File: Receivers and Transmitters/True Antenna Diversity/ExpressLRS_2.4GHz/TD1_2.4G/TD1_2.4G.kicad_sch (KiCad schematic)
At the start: 8 parts, among them J1 Conn_01x04_Pin, J2 Conn_01x04_Socket, U1 TPS7A4701xRGW

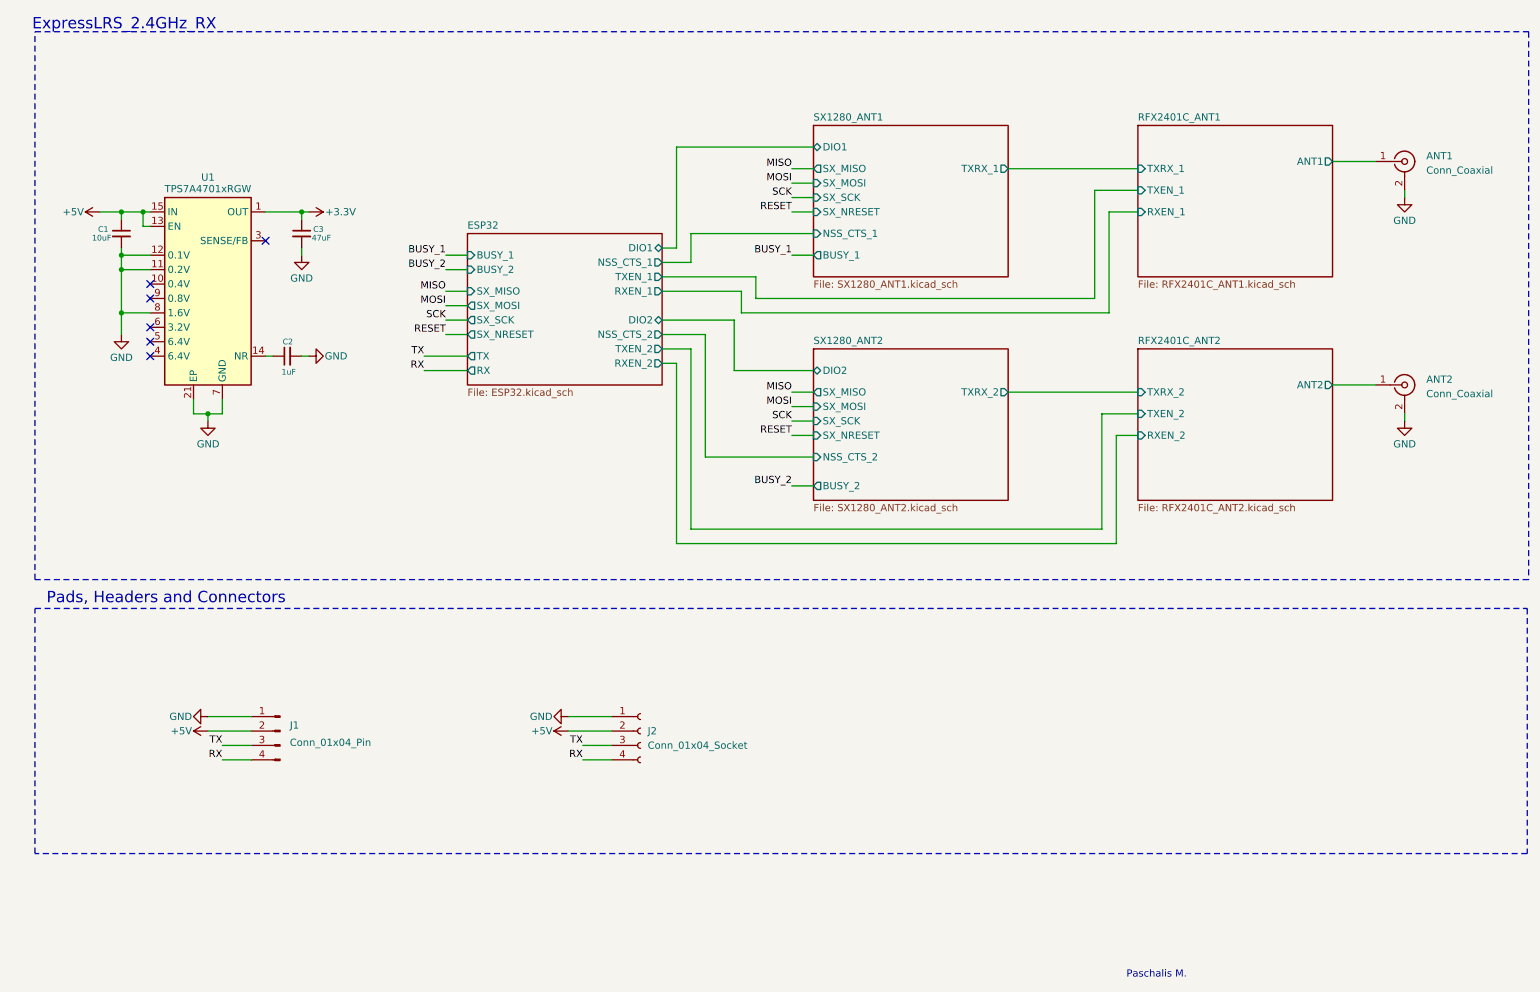
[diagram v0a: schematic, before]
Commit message: Update True Antenna Diversity TD1_2.4G KiCad schematics and PCB design
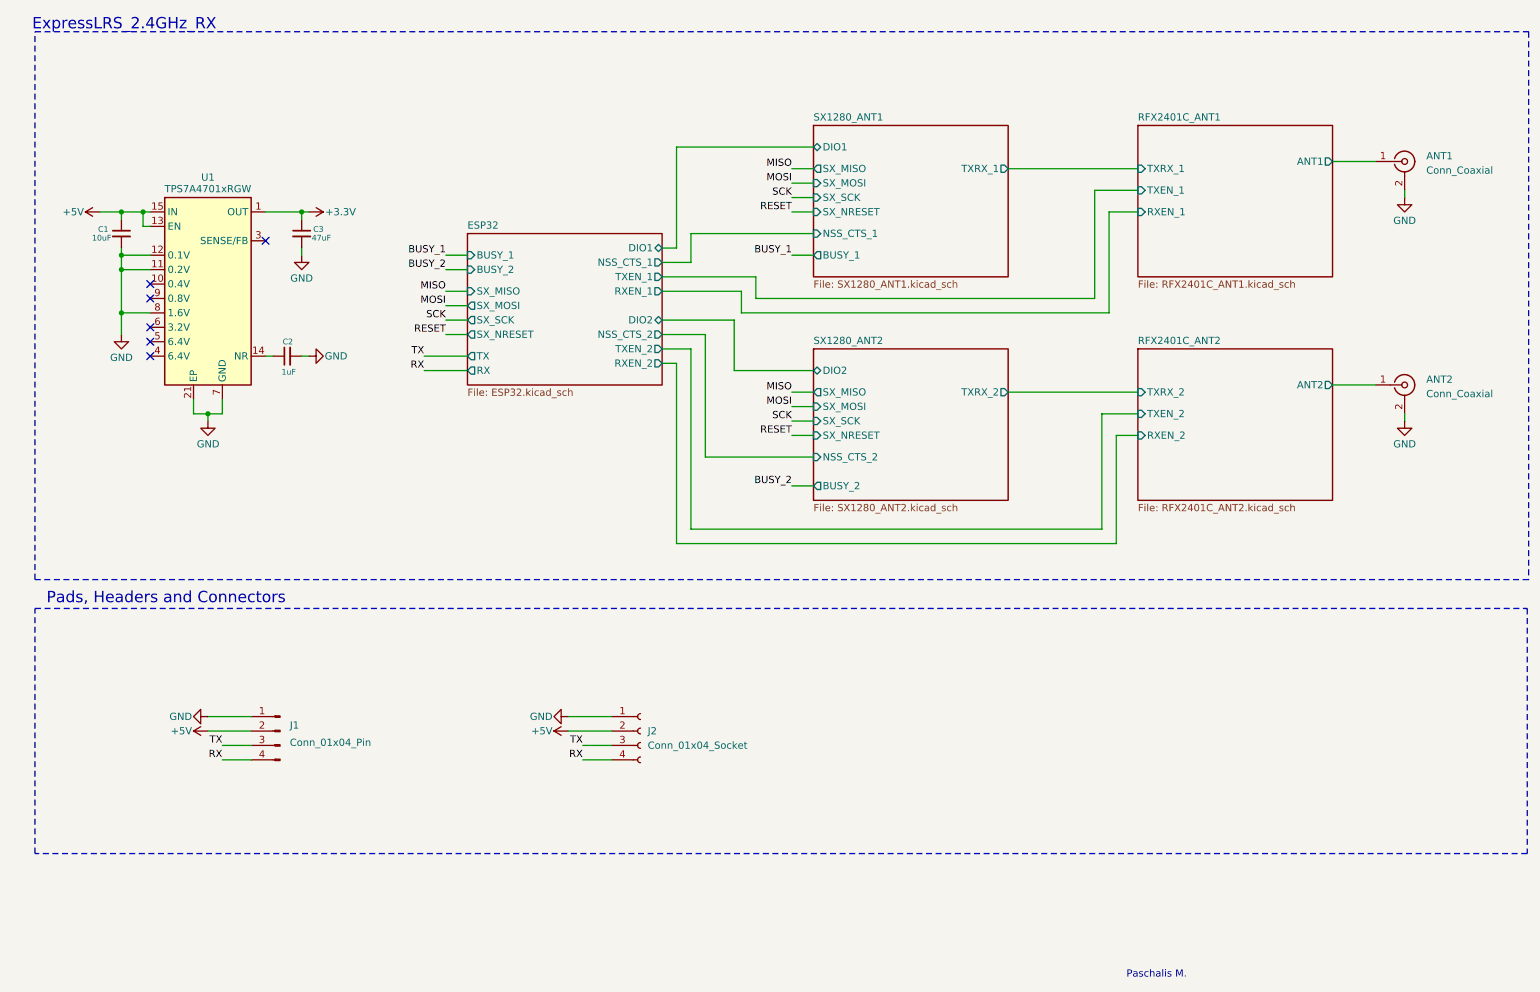
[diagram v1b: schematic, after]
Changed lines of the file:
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@@
 (kicad_sch
-	(version 20231120)
+	(version 20250114)
 	(generator "eeschema")
-	(generator_version "8.0")
+	(generator_version "9.0")
 	(paper "A4")
 	(title_block
@@
 		(comment 3 "The receiver utilizes two independent Semtech LoRa chips.")
 	)
+	(rectangle
+		(start 16.51 17.78)
+		(end 279.654 114.3)
+		(stroke
+			(width 0)
+			(type dash)
+		)
+		(fill
+			(type none)
+		)
+	)
+	(rectangle
+		(start 16.51 119.38)
+		(end 279.4 162.56)
+		(stroke
+			(width 0)
+			(type dash)
+		)
+		(fill
+			(type none)
+		)
+	)
+	(text "Pads, Headers and Connectors"
+		(exclude_from_sim no)
+		(at 39.624 117.602 0)
+		(effects
+			(font
+				(size 2 2)
+			)
+		)
+	)
+	(text "ExpressLRS_2.4GHz_RX"
+		(exclude_from_sim no)
+		(at 32.258 16.51 0)
+		(effects
+			(font
+				(face "Arial")
+				(size 2 2)
+				(thickness 0.2938)
+			)
+		)
+	)
+	(text "Paschalis M."
+		(exclude_from_sim no)
+		(at 214.122 183.896 0)
+		(effects
+			(font
+				(face "Arial")
+				(size 1.27 1.27)
+			)
+		)
+	)
 	(junction
 		(at 31.75 57.15)
@@
 		)
 	)
-	(rectangle
-		(start 16.51 17.78)
-		(end 279.654 114.3)
-		(stroke
-			(width 0)
-			(type dash)
-		)
-		(fill
-			(type none)
-		)
-	)
-	(rectangle
-		(start 16.51 119.38)
-		(end 279.4 162.56)
-		(stroke
-			(width 0)
-			(type dash)
-		)
-		(fill
-			(type none)
-		)
-	)
 	(image
 		(at 110.49 66.04)
@@
 			"f3jO+ZdPteZ1t1uyGQgBhABCACGAEEAIIAQQAggBhABCACGAEEAIIAQQAggBhABCACGAEEAIIAQQ"
 			"AggBhABCACGAEEAIIAQQAggBhABCACGAEEAIIAQQAggBhABCACGAEEAIIAQQAggBhABCACGAEEAI"
-			"IAQQAvTjoulnt9//jJQO30bYDQBKeAb44JfutQpZiQAAAABJRU5ErkJggg=="
-		)
-	)
-	(text "Pads, Headers and Connectors"
-		(exclude_from_sim no)
-		(at 39.624 117.602 0)
-		(effects
-			(font
-				(size 2 2)
-			)
-		)
-	)
-	(text "ExpressLRS_2.4GHz_RX"
-		(exclude_from_sim no)
-		(at 32.258 16.51 0)
-		(effects
-			(font
-				(face "Arial")
-				(size 2 2)
-				(thickness 0.2938)
-			)
-		)
-	)
-	(text "Paschalis M."
-		(exclude_from_sim no)
-		(at 214.122 183.896 0)
-		(effects
-			(font
-				(face "Arial")
-				(size 1.27 1.27)
-			)
+			"IAQQAvTjoulnt9//jJQO30bYDQBKeAb44JfutQpZiQAAAABJRU5ErkJggrAiA34dVgAAAgAAAQAA"
+			"AAAAAAAAAAAAAAAAAAAAAAAAAAAAABMAAAA4IwN+HVYAAGgiA34dVgAAAAAAAAAAAAAAAAAAAAAA"
+			"AAAAAADzAQAAaCIDfh1WAAAAAAAAAAAAAAAAAAAAAAAAeCMDfh1WAABQJAN+HVYAAAAAAAAAAAAA"
+			"YBrZ5NJyAAAAAAAAAAAAAEAjA34dVgAAAQAAAAAAAAAAAAAAAAAAAAAAAAAAAAAAAAAAAAoAAAAw"
+			"JAN+HVYAAPgiA34dVgAAAAAAAAAAAAAAAAAAAAAAAPgiA34dVgAAAAAAAAAAAABgGtnk0nIAAAAA"
+			"AAAAAAAAqCMDfh1WAAACAAABAAAAAAAAAAAAAAAAAAAAAAAAAAAAAAAACgAAAJgkA34dVgAAYCMD"
+			"fh1WAAAAAAAAAAAAAAAAAAAAAAAAAAAAEAwAAIBgIwN+HVYAAAAAAAAAAAAAAAAAAAAAAAAAAAAA"
+			"AAAAAAAAAAAAAAAAYBrZ5NJyAAAAAAAAAAAAADAkA34dVgAAAQAAAAAAAAAAAAAAAAAAAAAAAAAA"
+			"AAAAAAAAAAoAAAAAAAAAAAAAAOgjA34dVgAAAAAAAAAAAAAAAAAAAAAAAOgjA34dVgAAAAAAAAAA"
+			"AABgGtnk0nIAAAAAAAAAAAAAmCQDfh1WAAACAAABAAAAAAAAAAAAAAAAAAAAAAAAAAAAAAAACgAA"
+			"AAAAAAAAAAAAUCQDfh1WAAAAAAAAAAAAAAAAAAAAAAAAAAAAEA4AAIBQJAN+HVYAAAAAAAAAAAAA"
+			"AAAAAAAAAACwIAN+HVYAAMBz3H0dVgAAIOnW5NJyAACQc9x9HVYAACAlA34dVgAAAQAAAAAAAAAA"
+			"AAAAAAAAAAAAAAAAAAAAAAAAAJQRAAABAAB+HVYAANgkA34dVgAAAAAAAAAAAAAg6dbk0nIAAMgl"
+			"A34dVgAAAAAAAAAAAABAGdnk0nIAAAAAAAAAAAAAiCUDfh1WAAACAAABAAAAAAAAAAAAAAAAAAAA"
+			"AAAAAAAAAAAAEwAAABAmA34dVgAAQCUDfh1WAAAAAAAAAAAAAAAAAAAAAAAAAAAAAOcBAABAJQN+"
+			"HVYAAAAAAAAAAAAAAAAAAAAAAABQJgN+HVYAAAAAAAAAAAAAQBnZ5NJyAAAAAAAAAAAAABAmA34d"
+			"VgAAAgAAAQAAAAAAAAAAAAAAAAAAAAAAAAAAAAAAABMAAACYJgN+HVYAAMglA34dVgAAAAAAAAAA"
+			"AAAAAAAAAAAAAAAAAADoAQAAyCUDfh1WAAAAAAAAAAAAAAAAAAAAAAAA2CYDfh1WAAAAAAAAAAAA"
+			"AEAZ2eTScgAAAAAAAAAAAACYJgN+HVYAAAIAAAEAAAAAAAAAAAAAAAAAAAAAAAAAAAAAAAAAAAAA"
+			"AAAAAAAAAAAAAAAAAAAAAAAAAAAAAAAAAAAAAAAAAAAAAAAAAAAAAAAAAAAAAAAAAAAAAAAAAAAA"
+			"AAAAAAAAAAAAAAAAAAAAAAAAAAAAAAAAAAAAAAAAAAAAAAAAAAAAAAAAAAAAAAAAAAAAAAAAAAAA"
+			"AAAAAAAAAAAAAAAAAAAAAAAAAAAAAAAAAAAAAAAAAAAAAAAAAAAAAAAAAAAAAAAAAAAAAAAAAAAA"
+			"AAAAAAAAAAAAAAAAAAAAAAAAAAAAAAAAAAAAAAAAAAAAAAAAAAAAAAAAAAAAAAAAAAAAAAAAAAAA"
+			"AAAAAAAAAAAAAAAAAAAAAAAAAAAAAAAAAAAAAAAAAAAAAAAAAAAAAAAAAAAAAAAAAAAAAAAAAAAA"
+			"AAAAAAAAAAAAAAAAAAAAAAAAAAAAAAAAAAAAAAAAAAAAAAAAAAAAAAAAAAAAAAAAAAAAAAAAAAAA"
+			"AAAAAAAAAAAAAAAAAAAAAAAAAAAAAAAAAAAAAAAAAAAAAAAAAAAAAAAAAAAAAAAAAAAAAAAAAAAA"
+			"AAAAAAAAAAAAAAAAAAAAAAAAAAAAAAAAAAAAAAAAAAAAAAAAAAAAAAAAAAAAAAAAAAAAAAAAAAAA"
+			"AAAAAAAAAAAAAAAAAAAAAAAAAAAAAAAAAAAAAAAAAAAAAAAAAAAAAAAAAAAAAAAAAAAAAAAAAAAA"
+			"AAAAAAAAAAAAAAAAAAAAAAAAAAAAAAAAAAAAAAAAAAAAAAAAAAAAAAAAAAAAAAAAAAAAAAAAAAAA"
+			"AAAAAAAAAAAAAAAAAAAAAAAAAAAAAAAAAAAAAAAAAAAAAAAAAAAAAAAAAAAAAAAAAAAAAAAAAAAA"
+			"AAAAAAAAAAAAAAAAAAAAAAAAAAAAAAAAAAAAAAAAAAAAAAAAAAAAAAAAAAAAAAAAAAAAAAAAAAAA"
+			"AAAAAAAAAAAAAAAAAAAAAAAAAAAAAAAAAAAAAAAAAAAAAAAAAAAAAAAAAAAAAAAAAAAAAAAAAAAA"
+			"AAAAAAAAAAAAAAAAAAAAAAAAAAAAAAAAAAAAAAAAAAAAAAAAAAAAAAAAAAAAAAAAAAAAAAAAAAAA"
+			"AAAAAAAAAAAAAAAAAAAAAAAAAAAAAAAAAAAAAAAAAAAAAAAAAAAAAAAAAAAAAAAAAAAAAAAAAAAA"
+			"AAAAAAAAAAAAAAAAAAAAAAAAAAAAAAAAAAAAAAAAAAAAAAAAAAAAAAAAAAAAAAAAAAAAAAAAAAAA"
+			"AAAAAAAAAAAAAAAAAAAAAAAAAAAAAAAAAAAAAAAAAAAAAAAAAAAAAAAAAAAAAAAAAAAAAAAAAAAA"
+			"AAAAAAAAAAAAAAAAAAAAAAAAAAAAAAAAAAAAAAAAAAAAAAAAAAAAAAAAAA=="
 		)
 	)
@@
 		(at 210.82 34.29)
 		(size 34.29 26.67)
+		(exclude_from_sim no)
+		(in_bom yes)
+		(on_board yes)
+		(dnp no)
 		(fields_autoplaced yes)
 		(stroke
@@
 		(at 153.67 34.29)
 		(size 34.29 26.67)
+		(exclude_from_sim no)
+		(in_bom yes)
+		(on_board yes)
+		(dnp no)
 		(fields_autoplaced yes)
 		(stroke
@@
 		(at 92.71 53.34)
 		(size 34.29 26.67)
+		(exclude_from_sim no)
+		(in_bom yes)
+		(on_board yes)
+		(dnp no)
 		(fields_autoplaced yes)
 		(stroke
@@
 		(at 210.82 73.66)
 		(size 34.29 26.67)
+		(exclude_from_sim no)
+		(in_bom yes)
+		(on_board yes)
+		(dnp no)
 		(fields_autoplaced yes)
 		(stroke
@@
 		(at 153.67 73.66)
 		(size 34.29 26.67)
+		(exclude_from_sim no)
+		(in_bom yes)
+		(on_board yes)
+		(dnp no)
 		(fields_autoplaced yes)
 		(stroke
@@
 		)
 	)
+	(embedded_fonts no)
 )
